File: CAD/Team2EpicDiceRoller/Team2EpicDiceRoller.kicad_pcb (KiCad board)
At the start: 2 copper layers, 90 x 110 mm, 77 parts, among them J1 Conn_02x03_Odd_Even, J2 Conn_01x16, J3 Barrel_Jack, Q1 BSS138, SW1 SW_Toggle_SPDT, SW2 Tilt_Switch, SW3 SW_Power, SW4 RotaryEncoder_Switch, SW5 SW_LeftMenu, SW6 SW_MidMenu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

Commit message: started route
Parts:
- C13, C15: moved to B.Cu
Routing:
- net AD1_PC1: track 0.00 -> 37.3 mm, vias 0 -> 2
- net RESET#: track 0.00 -> 35.5 mm
- net AD0_PC0: track 0.00 -> 19.9 mm
- net IO5_PD5: track 0.00 -> 18.7 mm
- net /EncDebnc: track 0.00 -> 18.0 mm
- net IO6_PD6: track 0.00 -> 15.9 mm
- net Net-(R22-Pad2): track 0.00 -> 5.72 mm
- net Net-(R21-Pad1): track 0.00 -> 5.66 mm
- net Net-(R4-Pad2): track 0.00 -> 5.25 mm
- added copper zone on F.Cu, net +BATT

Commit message: route in progress
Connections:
- C16 pad 1: VCC -> Net-(C16-Pad1)
- C6 pad 1: VCC -> Net-(C16-Pad1)
- JP2 pad 2: VCC -> Net-(C16-Pad1)
- L1 pad 2: VCC -> Net-(C16-Pad1)
- RV1 pad 1: VCC -> Net-(C16-Pad1)
- TP1 pad 1: VCC -> Net-(C16-Pad1)
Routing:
- net /Vin: track 0.00 -> 160.5 mm
- net VCC: track 0.00 -> 96.0 mm, vias 0 -> 4
- net +3V3: track 0.00 -> 79.9 mm
- net Net-(R4-Pad2): track 5.25 -> 84.9 mm, vias 0 -> 2
- net IO9_PB1: track 0.00 -> 66.2 mm
- net Net-(C16-Pad1): track 0.00 -> 66.2 mm
- net /3V3: track 0.00 -> 64.1 mm
- net /RigDebn: track 0.00 -> 48.5 mm, vias 0 -> 2
- net AD3_PC3: track 0.00 -> 37.5 mm
- net AD2_PC2: track 0.00 -> 37.5 mm
- net IO11_MOSI_PB3: track 0.00 -> 35.1 mm
- net IO13_SCK_PB5: track 0.00 -> 29.0 mm
- net IO12_MISO_PB4: track 0.00 -> 29.0 mm
- net Net-(D1-Pad1): track 0.00 -> 25.3 mm
- net /LeftDebn: track 0.00 -> 24.9 mm
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
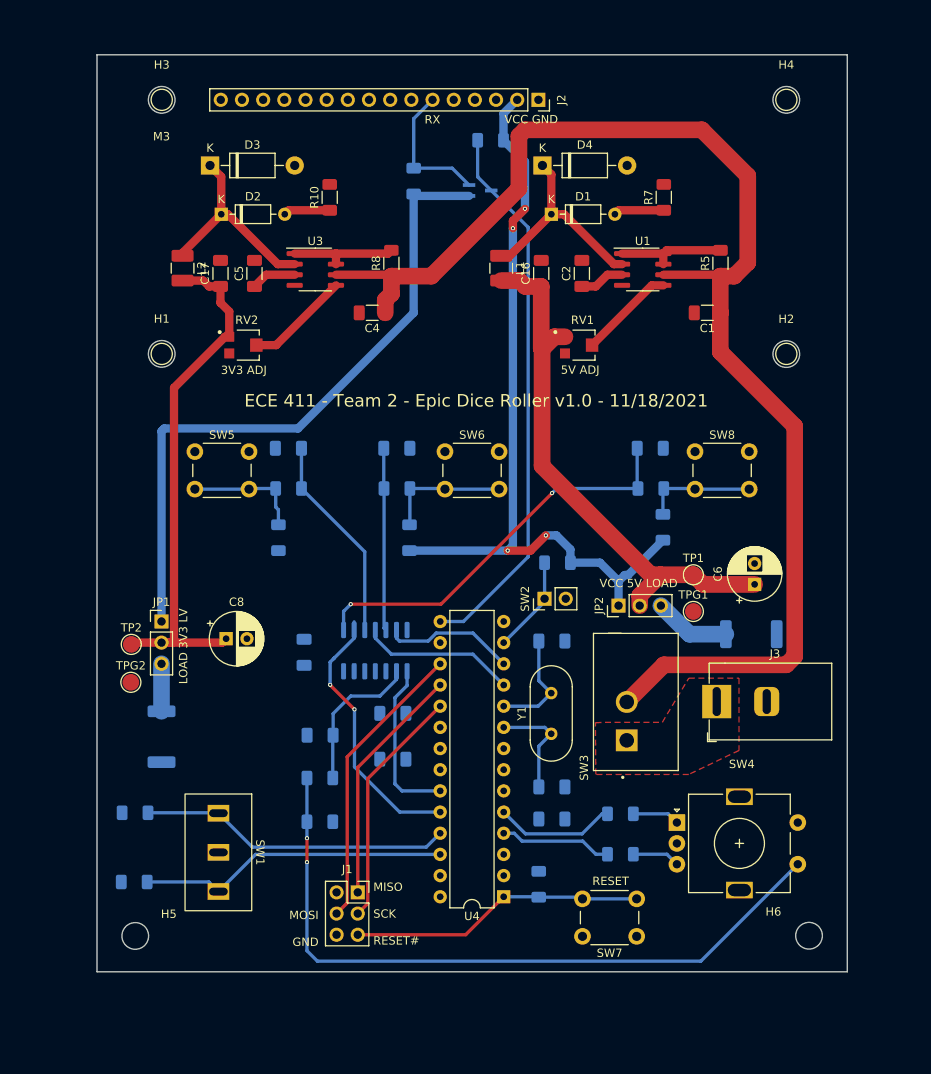
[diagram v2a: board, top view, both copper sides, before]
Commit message: Found another issue, inductors silkscreen conflicted with capacitors
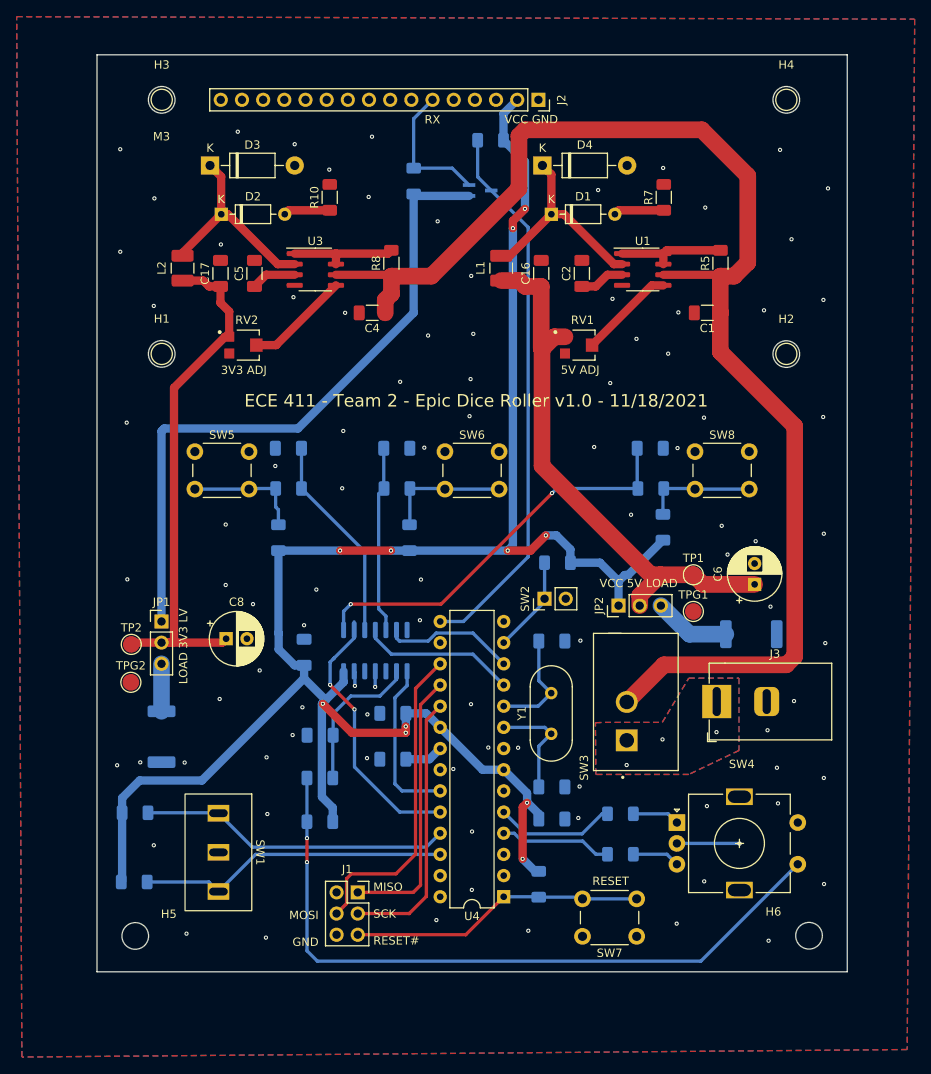
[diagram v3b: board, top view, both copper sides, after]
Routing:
- net VCC: track 96.0 -> 236.4 mm, vias 4 -> 11
- net GND: track 0.00 -> 11.2 mm, vias 0 -> 94
- net Net-(C13-Pad2): track 0.00 -> 4.65 mm
- net IO12_MISO_PB4: track 29.0 -> 32.9 mm
- net IO13_SCK_PB5: track 29.0 -> 32.6 mm
- net IO11_MOSI_PB3: track 35.1 -> 38.2 mm
- net /MidDebn: track 21.9 -> 22.4 mm
- net +BATT: vias 0 -> 3
- added copper zone on B.Cu, net +BATT
- added copper zone on B.Cu, net GND
- added copper zone on F.Cu, net GND

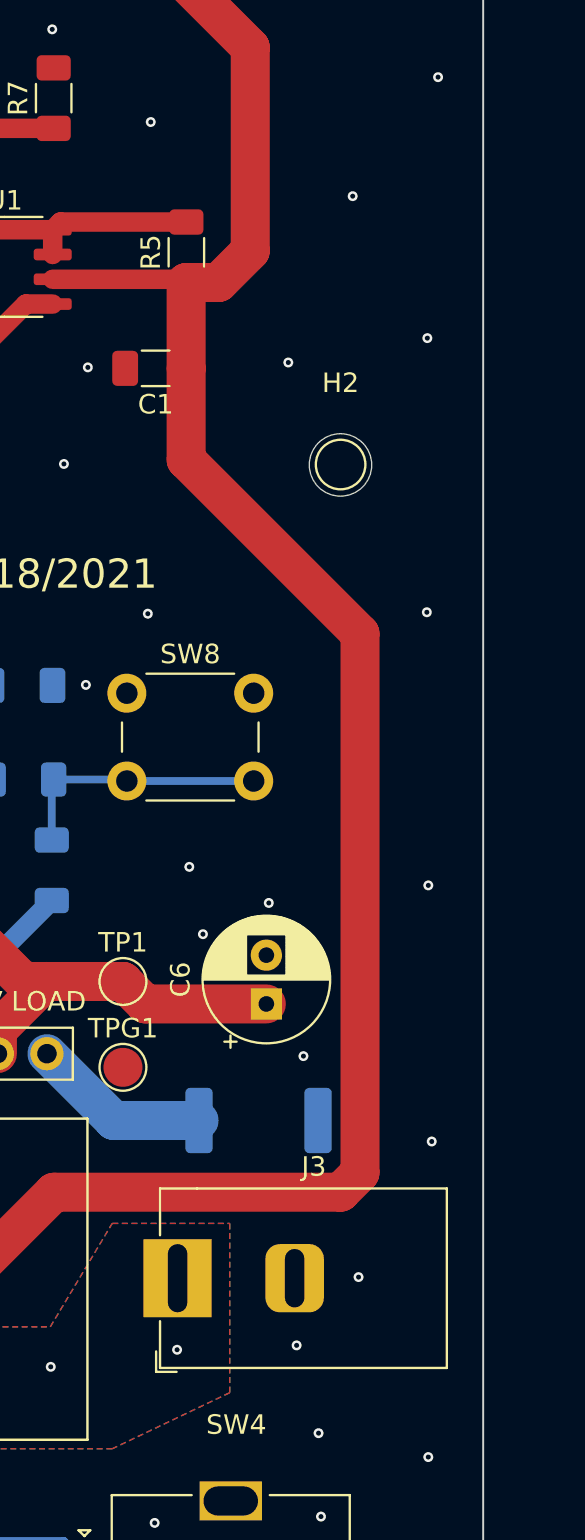
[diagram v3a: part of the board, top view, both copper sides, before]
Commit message: added qr code and symbol for power supply jack
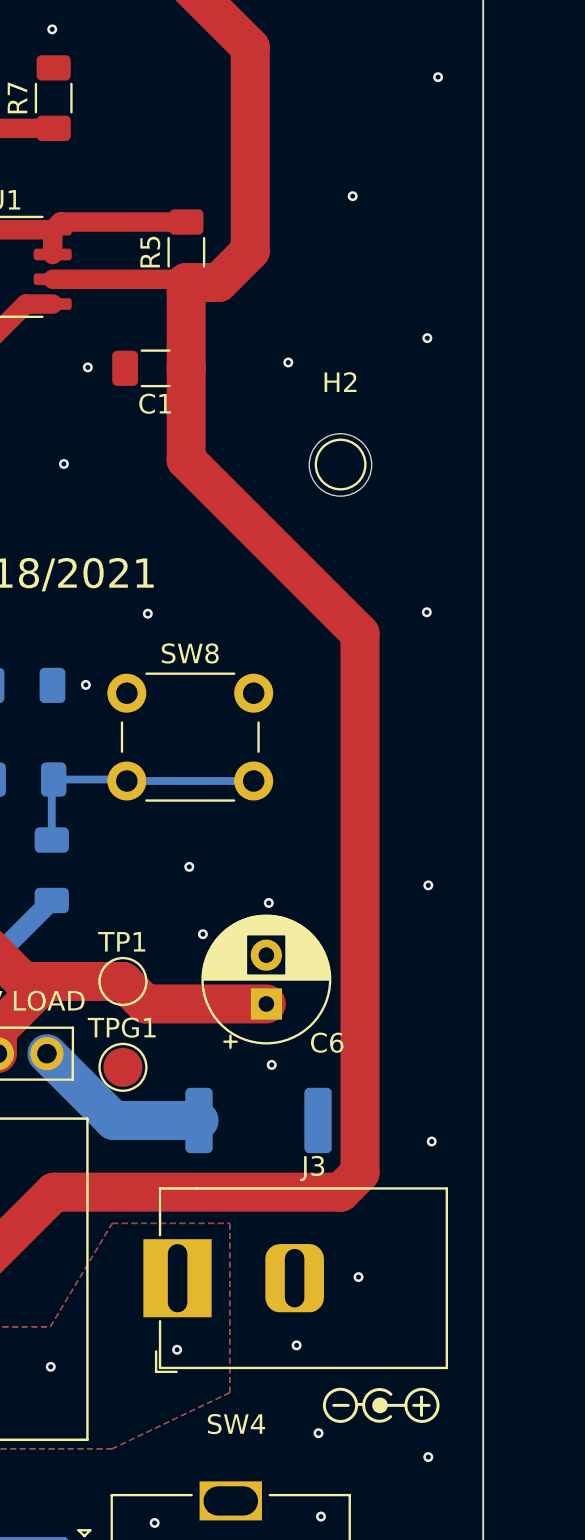
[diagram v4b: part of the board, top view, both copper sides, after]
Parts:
- added G***: LOGO, Graphics:qr, B.Cu at (170.7, 42.4)
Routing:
- net GND: vias 94 -> 93

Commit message: updated pcb and added dice graphic
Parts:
- added G***: LOGO, Graphics:d20, F.Cu at (141.9, 78.5)

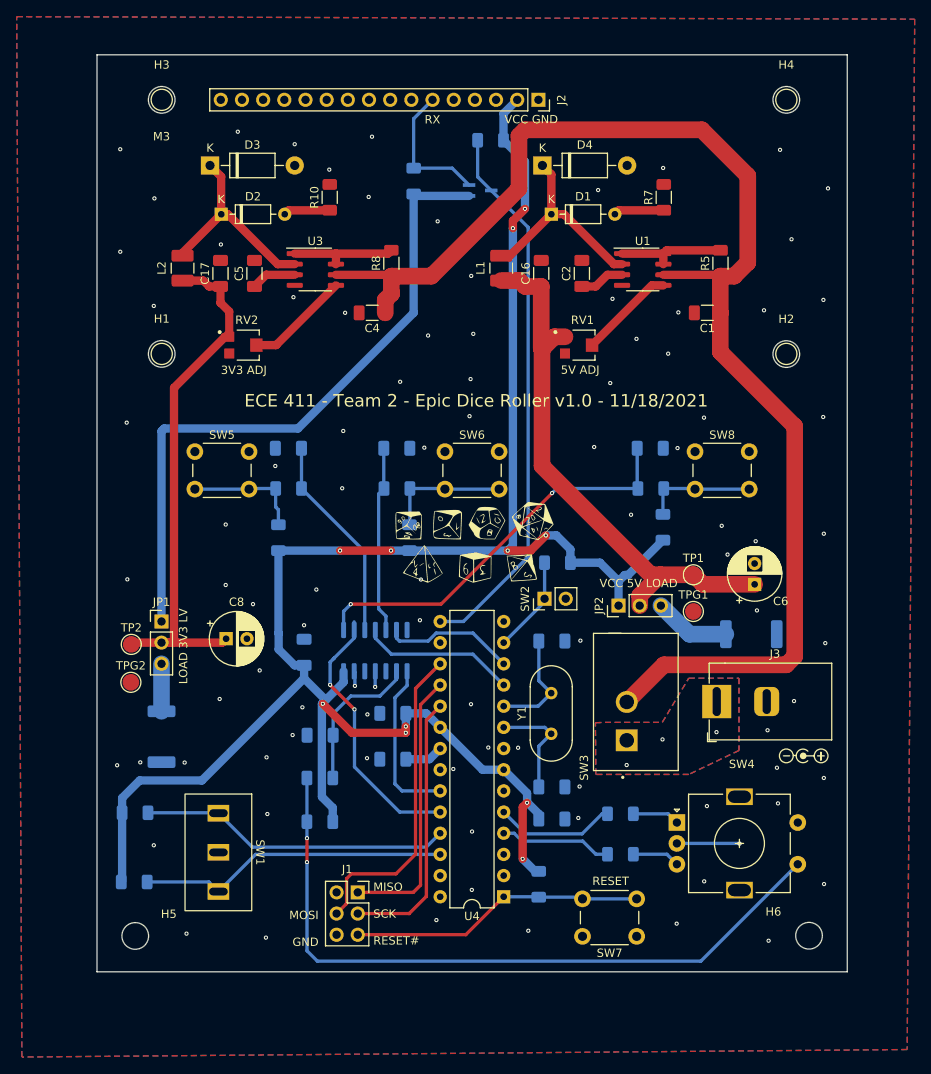
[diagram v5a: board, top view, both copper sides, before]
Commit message: Fixed DRC failures, tiny traces, circles on silkscreen holes
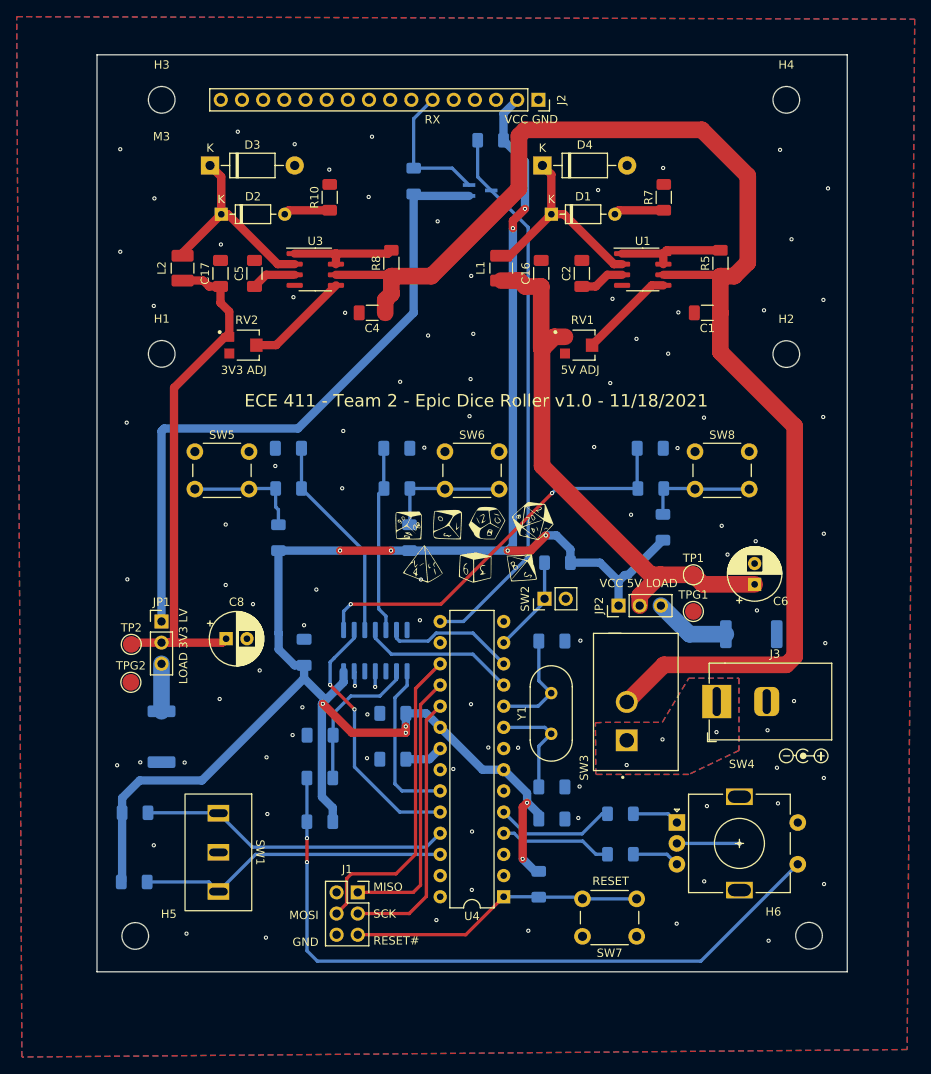
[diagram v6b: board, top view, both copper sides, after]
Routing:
- net AD1_PC1: track 32.5 -> 31.4 mm
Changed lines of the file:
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@@
     (fp_line (start 1.33 -1.33) (end 1.33 0) (layer "F.SilkS") (width 0.12))
     (fp_line (start 0 -1.33) (end 1.33 -1.33) (layer "F.SilkS") (width 0.12))
-    (fp_circle (center 0 -29.7434) (end 1.27 -29.7434) (layer "F.SilkS") (width 0.12) (fill none))
-    (fp_circle (center 0 45.1866) (end 1.27 45.1866) (layer "F.SilkS") (width 0.12) (fill none))
-    (fp_circle (center 30.48 45.1866) (end 31.75 45.1866) (layer "F.SilkS") (width 0.12) (fill none))
-    (fp_circle (center 30.48 -29.7434) (end 31.75 -29.7434) (layer "F.SilkS") (width 0.12) (fill none))
     (fp_line (start -1.8 -1.8) (end 1.75 -1.8) (layer "F.CrtYd") (width 0.05))
     (fp_line (start 1.75 -1.8) (end 1.75 39.9) (layer "F.CrtYd") (width 0.05))
@@
     (fp_line (start 0.635 -1.27) (end 1.27 -0.635) (layer "F.Fab") (width 0.1))
     (fp_line (start -2.54 -32.2834) (end 33.02 -32.2834) (layer "F.Fab") (width 0.12))
+    (fp_circle (center 0 -29.7434) (end 1.27 -29.7434) (layer "F.Fab") (width 0.12) (fill none))
+    (fp_circle (center 0 45.1866) (end 1.27 45.1866) (layer "F.Fab") (width 0.12) (fill none))
+    (fp_circle (center 30.48 45.1866) (end 31.75 45.1866) (layer "F.Fab") (width 0.12) (fill none))
+    (fp_circle (center 30.48 -29.7434) (end 31.75 -29.7434) (layer "F.Fab") (width 0.12) (fill none))
     (pad "1" thru_hole rect (at 0 0 270) (size 1.7 1.7) (drill 1) (layers *.Cu *.Mask)
-      (net 1 "GND") (pinfunction "Pin_1") (pintype "passive"))
+      (net 1 "GND") (pinfunction "Pin_1"))
     (pad "2" thru_hole oval (at 0 2.54 270) (size 1.7 1.7) (drill 1) (layers *.Cu *.Mask)
-      (net 4 "VCC") (pinfunction "Pin_2") (pintype "passive"))
+      (net 4 "VCC") (pinfunction "Pin_2"))
     (pad "3" thru_hole oval (at 0 5.08 270) (size 1.7 1.7) (drill 1) (layers *.Cu *.Mask)
-      (net 13 "unconnected-(J2-Pad3)") (pinfunction "Pin_3") (pintype "passive+no_connect"))
+      (net 13 "unconnected-(J2-Pad3)") (pinfunction "Pin_3"))
     (pad "4" thru_hole oval (at 0 7.62 270) (size 1.7 1.7) (drill 1) (layers *.Cu *.Mask)
-      (net 14 "unconnected-(J2-Pad4)") (pinfunction "Pin_4") (pintype "passive+no_connect"))
+      (net 14 "unconnected-(J2-Pad4)") (pinfunction "Pin_4"))
     (pad "5" thru_hole oval (at 0 10.16 270) (size 1.7 1.7) (drill 1) (layers *.Cu *.Mask)
-      (net 15 "unconnected-(J2-Pad5)") (pinfunction "Pin_5") (pintype "passive+no_connect"))
+      (net 15 "unconnected-(J2-Pad5)") (pinfunction "Pin_5"))
     (pad "6" thru_hole oval (at 0 12.7 270) (size 1.7 1.7) (drill 1) (layers *.Cu *.Mask)
-      (net 51 "LCD_RX") (pinfunction "Pin_6") (pintype "passive"))
+      (net 51 "LCD_RX") (pinfunction "Pin_6"))
     (pad "7" thru_hole oval (at 0 15.24 270) (size 1.7 1.7) (drill 1) (layers *.Cu *.Mask)
-      (net 17 "unconnected-(J2-Pad7)") (pinfunction "Pin_7") (pintype "passive+no_connect"))
+      (net 17 "unconnected-(J2-Pad7)") (pinfunction "Pin_7"))
     (pad "8" thru_hole oval (at 0 17.78 270) (size 1.7 1.7) (drill 1) (layers *.Cu *.Mask)
-      (net 18 "unconnected-(J2-Pad8)") (pinfunction "Pin_8") (pintype "passive+no_connect"))
+      (net 18 "unconnected-(J2-Pad8)") (pinfunction "Pin_8"))
     (pad "9" thru_hole oval (at 0 20.32 270) (size 1.7 1.7) (drill 1) (layers *.Cu *.Mask)
-      (net 19 "unconnected-(J2-Pad9)") (pinfunction "Pin_9") (pintype "passive+no_connect"))
+      (net 19 "unconnected-(J2-Pad9)") (pinfunction "Pin_9"))
     (pad "10" thru_hole oval (at 0 22.86 270) (size 1.7 1.7) (drill 1) (layers *.Cu *.Mask)
-      (net 20 "unconnected-(J2-Pad10)") (pinfunction "Pin_10") (pintype "passive+no_connect"))
+      (net 20 "unconnected-(J2-Pad10)") (pinfunction "Pin_10"))
     (pad "11" thru_hole oval (at 0 25.4 270) (size 1.7 1.7) (drill 1) (layers *.Cu *.Mask)
-      (net 21 "unconnected-(J2-Pad11)") (pinfunction "Pin_11") (pintype "passive+no_connect"))
+      (net 21 "unconnected-(J2-Pad11)") (pinfunction "Pin_11"))
     (pad "12" thru_hole oval (at 0 27.94 270) (size 1.7 1.7) (drill 1) (layers *.Cu *.Mask)
-      (net 22 "unconnected-(J2-Pad12)") (pinfunction "Pin_12") (pintype "passive+no_connect"))
+      (net 22 "unconnected-(J2-Pad12)") (pinfunction "Pin_12"))
     (pad "13" thru_hole oval (at 0 30.48 270) (size 1.7 1.7) (drill 1) (layers *.Cu *.Mask)
-      (net 23 "unconnected-(J2-Pad13)") (pinfunction "Pin_13") (pintype "passive+no_connect"))
+      (net 23 "unconnected-(J2-Pad13)") (pinfunction "Pin_13"))
     (pad "14" thru_hole oval (at 0 33.02 270) (size 1.7 1.7) (drill 1) (layers *.Cu *.Mask)
-      (net 24 "unconnected-(J2-Pad14)") (pinfunction "Pin_14") (pintype "passive+no_connect"))
+      (net 24 "unconnected-(J2-Pad14)") (pinfunction "Pin_14"))
     (pad "15" thru_hole oval (at 0 35.56 270) (size 1.7 1.7) (drill 1) (layers *.Cu *.Mask)
-      (net 25 "unconnected-(J2-Pad15)") (pinfunction "Pin_15") (pintype "passive+no_connect"))
+      (net 25 "unconnected-(J2-Pad15)") (pinfunction "Pin_15"))
     (pad "16" thru_hole oval (at 0 38.1 270) (size 1.7 1.7) (drill 1) (layers *.Cu *.Mask)
-      (net 26 "unconnected-(J2-Pad16)") (pinfunction "Pin_16") (pintype "passive+no_connect"))
+      (net 26 "unconnected-(J2-Pad16)") (pinfunction "Pin_16"))
     (model "${KICAD6_3DMODEL_DIR}/Connector_PinSocket_2.54mm.3dshapes/PinSocket_1x16_P2.54mm_Vertical.wrl"
       (offset (xyz 0 0 0))
@@
   (segment (start 100.025 109.15) (end 102.125 107.05) (width 1) (layer "B.Cu") (net 4))
   (segment (start 102.125 107.05) (end 109.6 107.05) (width 1) (layer "B.Cu") (net 4))
-  (segment (start 146.9 40.8) (end 146.901911 40.801911) (width 1) (layer "B.Cu") (net 4))
   (segment (start 134.5 79.475) (end 146.275 79.475) (width 1) (layer "B.Cu") (net 4))
   (segment (start 120.7125 93.2375) (end 121.85 93.2375) (width 1) (layer "B.Cu") (net 4))
@@
   (segment (start 125.467499 92.367499) (end 127.86 89.974999) (width 0.4) (layer "B.Cu") (net 28))
   (segment (start 127.86 89.974999) (end 127.86 89) (width 0.4) (layer "B.Cu") (net 28))
-  (segment (start 125.467499 92.367499) (end 125.359999 92.475) (width 0.4) (layer "B.Cu") (net 28))
-  (segment (start 127.86 88.025001) (end 127.86 89) (width 0.4) (layer "B.Cu") (net 28))
   (segment (start 124.975 95.575) (end 124.975 92.859998) (width 0.4) (layer "B.Cu") (net 28))
   (segment (start 132.75 97.125) (end 132.75 107.45) (width 0.4) (layer "B.Cu") (net 29))
@@
   (segment (start 115.325 72.025) (end 115.25 72.1) (width 0.4) (layer "B.Cu") (net 55))
   (segment (start 118.445 72.025) (end 118.445 74.245) (width 0.4) (layer "B.Cu") (net 55))
-  (segment (start 118.445 72.025) (end 118.445 71.97) (width 0.4) (layer "B.Cu") (net 55))
-  (segment (start 118.445 71.97) (end 118.375 71.9) (width 0.4) (layer "B.Cu") (net 55))
   (segment (start 118.445 72.025) (end 115.325 72.025) (width 0.4) (layer "B.Cu") (net 55))
   (segment (start 118.445 74.245) (end 118.775 74.575) (width 0.4) (layer "B.Cu") (net 55))

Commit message: final adjustments
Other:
- rule pad_to_mask_clearance: 0.0508 -> 0
